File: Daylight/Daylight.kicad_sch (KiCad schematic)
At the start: 28 parts, among them J1 Conn_01x02_Female, J2 Conn_01x02_Female

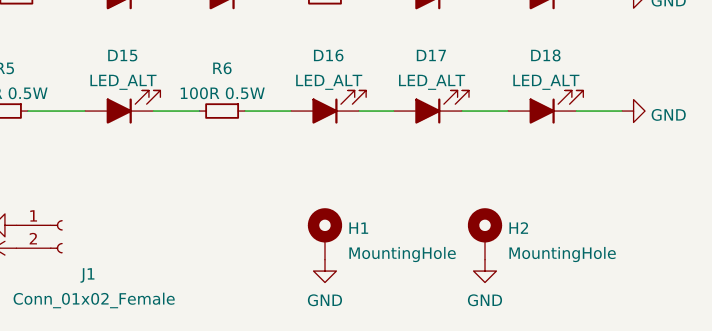
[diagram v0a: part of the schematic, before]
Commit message: Flipped leds for DFH
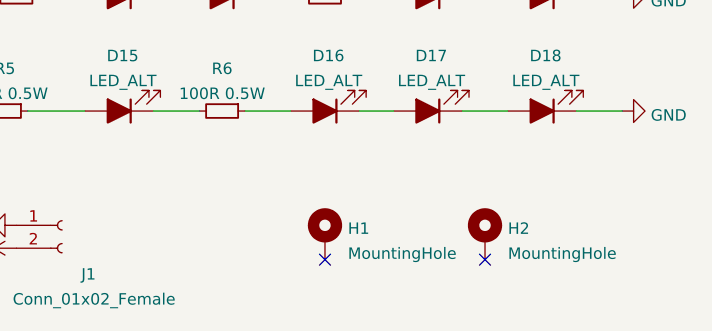
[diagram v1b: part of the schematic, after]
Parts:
- D1, D10, D11, D12, D13, D14, D15, D16, D17, D18, D2, D3, D4, D5, D6, D7, D8, D9: footprint Daylight:LED_PLCC_2835_Handsoldering -> Daylight:LED_PLCC_2835_Handsoldering_flipped
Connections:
- net GND: no longer H1.1, H2.1
- no-connect marks 0 -> 2
